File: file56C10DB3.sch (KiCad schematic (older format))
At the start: 31 parts, among them P1 BL_PAD, P10 CONN_01X01, P2 SWD_DAT, P3 SWD_CLK, P4 SWD_3V3, P5 SWD_GND, P6 SWD_RST, P7 CONN_01X01, P8 CONN_01X01, P9 CONN_01X01, U5 SAMD21E17A, Y1 32.768kHz

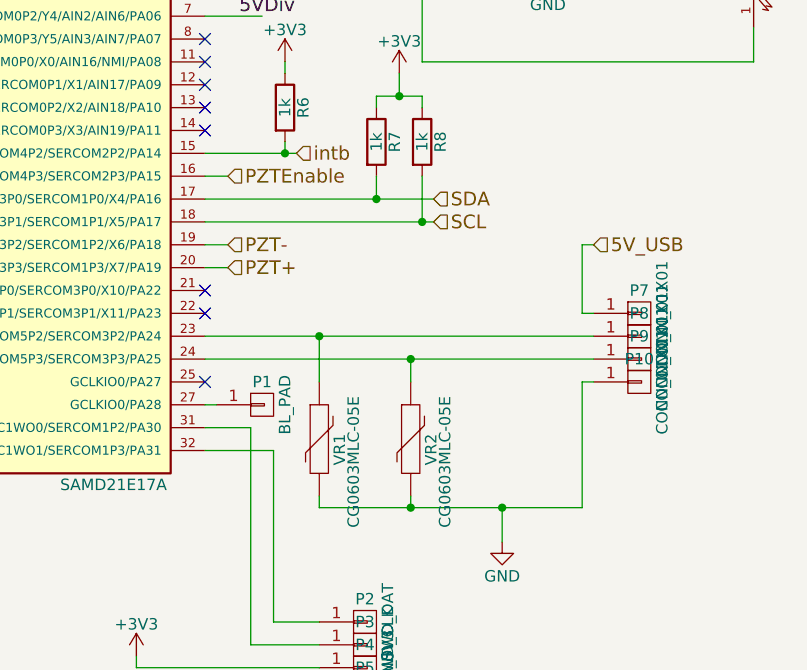
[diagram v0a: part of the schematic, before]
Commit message: Added outline for AAA battery size
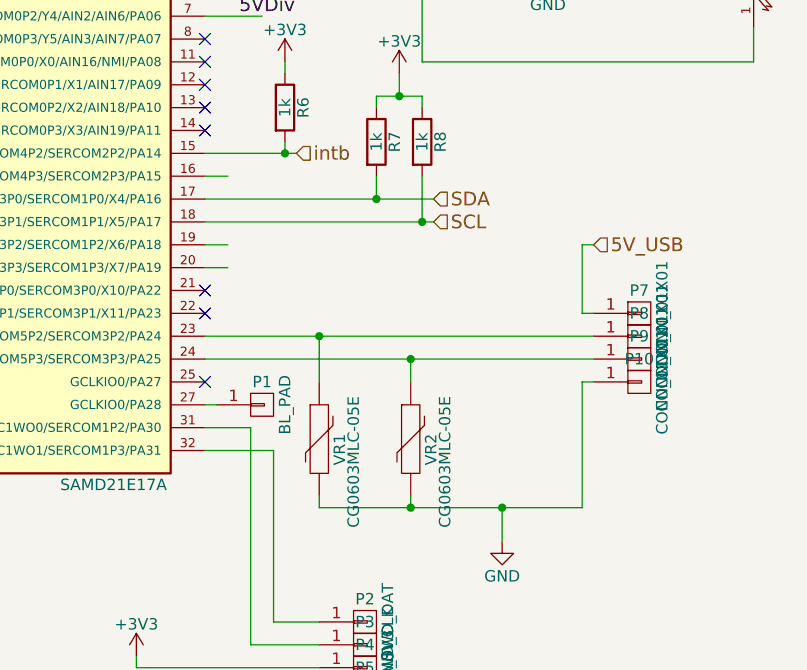
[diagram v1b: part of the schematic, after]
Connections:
- net labels removed: PZT+, PZT-, PZTEnable
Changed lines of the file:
@@
 $Descr A4 11693 8268
 encoding utf-8
-Sheet 6 6
+Sheet 6 7
 Title ""
 Date ""
@@
 Text HLabel 8050 3650 2    60   Input ~ 0
 SCL
-Text HLabel 7150 3850 2    60   Input ~ 0
-PZT+
-Text HLabel 7150 3750 2    60   Input ~ 0
-PZT-
 Text HLabel 2100 3900 0    60   Input ~ 0
 VbatIN
@@
 	8700 4050 8750 4050
 $Comp
-L GND #PWR01
+L GND #PWR15
 U 1 1 56C13132
 P 8350 5050
-F 0 "#PWR01" H 8350 4800 50  0001 C CNN
+F 0 "#PWR15" H 8350 4800 50  0001 C CNN
 F 1 "GND" H 8350 4900 50  0000 C CNN
 F 2 "" H 8350 5050 50  0000 C CNN
@@
 	8750 4350 8700 4350
 Wire Wire Line
-	8700 4350 8700 4900
+	8700 4900 8700 4350
 Wire Wire Line
 	8350 4900 8350 5050
@@
 Connection ~ 3600 2550
 $Comp
-L GND #PWR02
+L GND #PWR5
 U 1 1 56C1336E
 P 3300 3150
-F 0 "#PWR02" H 3300 2900 50  0001 C CNN
+F 0 "#PWR5" H 3300 2900 50  0001 C CNN
 F 1 "GND" H 3300 3000 50  0000 C CNN
 F 2 "" H 3300 3150 50  0000 C CNN
@@
 $EndComp
 $Comp
-L GND #PWR03
+L GND #PWR6
 U 1 1 56C133A0
 P 3600 3150
-F 0 "#PWR03" H 3600 2900 50  0001 C CNN
+F 0 "#PWR6" H 3600 2900 50  0001 C CNN
 F 1 "GND" H 3600 3000 50  0000 C CNN
 F 2 "" H 3600 3150 50  0000 C CNN
@@
 $EndComp
 $Comp
-L GND #PWR04
+L GND #PWR8
 U 1 1 56C133D2
 P 3900 3150
-F 0 "#PWR04" H 3900 2900 50  0001 C CNN
+F 0 "#PWR8" H 3900 2900 50  0001 C CNN
 F 1 "GND" H 3900 3000 50  0000 C CNN
 F 2 "" H 3900 3150 50  0000 C CNN
@@
 Wire Wire Line
 	3900 3050 3900 3150
-Text HLabel 7150 3450 2    60   Input ~ 0
-PZTEnable
 $Comp
 L R R7
@@
 $EndComp
 $Comp
-L +3V3 #PWR05
+L +3V3 #PWR14
 U 1 1 56C24D00
 P 7900 3000
-F 0 "#PWR05" H 7900 2850 50  0001 C CNN
+F 0 "#PWR14" H 7900 2850 50  0001 C CNN
 F 1 "+3V3" H 7900 3140 50  0000 C CNN
 F 2 "" H 7900 3000 50  0000 C CNN
@@
 	7950 4850 7950 4900
 Wire Wire Line
-	8700 4900 7550 4900
+	7550 4900 8700 4900
 Connection ~ 8350 4900
 Wire Wire Line
@@
 Connection ~ 8550 2250
 $Comp
-L GND #PWR06
+L GND #PWR16
 U 1 1 56C269FF
 P 8550 2550
-F 0 "#PWR06" H 8550 2300 50  0001 C CNN
+F 0 "#PWR16" H 8550 2300 50  0001 C CNN
 F 1 "GND" H 8550 2400 50  0000 C CNN
 F 2 "" H 8550 2550 50  0000 C CNN
@@
 5VDiv
 $Comp
-L GND #PWR07
+L GND #PWR1
 U 1 1 56C27864
 P 1600 4900
-F 0 "#PWR07" H 1600 4650 50  0001 C CNN
+F 0 "#PWR1" H 1600 4650 50  0001 C CNN
 F 1 "GND" H 1600 4750 50  0000 C CNN
 F 2 "" H 1600 4900 50  0000 C CNN
@@
 $EndComp
 $Comp
-L GND #PWR08
+L GND #PWR2
 U 1 1 56C278AB
 P 2350 4900
-F 0 "#PWR08" H 2350 4650 50  0001 C CNN
+F 0 "#PWR2" H 2350 4650 50  0001 C CNN
 F 1 "GND" H 2350 4750 50  0000 C CNN
 F 2 "" H 2350 4900 50  0000 C CNN
@@
 	2950 3500 2950 3700
 $Comp
-L GND #PWR09
+L GND #PWR4
 U 1 1 56C282F2
 P 2950 4100
-F 0 "#PWR09" H 2950 3850 50  0001 C CNN
+F 0 "#PWR4" H 2950 3850 50  0001 C CNN
 F 1 "GND" H 2950 3950 50  0000 C CNN
 F 2 "" H 2950 4100 50  0000 C CNN
@@
 	2950 4000 2950 4100
 $Comp
-L +3V3 #PWR010
+L +3V3 #PWR3
 U 1 1 56C28419
 P 2950 3500
-F 0 "#PWR010" H 2950 3350 50  0001 C CNN
+F 0 "#PWR3" H 2950 3350 50  0001 C CNN
 F 1 "+3V3" H 2950 3640 50  0000 C CNN
 F 2 "" H 2950 3500 50  0000 C CNN
@@
 	4000 2150 4000 2050
 $Comp
-L +3V3 #PWR011
+L +3V3 #PWR9
 U 1 1 56C28F33
 P 4000 1650
-F 0 "#PWR011" H 4000 1500 50  0001 C CNN
+F 0 "#PWR9" H 4000 1500 50  0001 C CNN
 F 1 "+3V3" H 4000 1790 50  0000 C CNN
 F 2 "" H 4000 1650 50  0000 C CNN
@@
 	7050 3350 7450 3350
 $Comp
-L +3V3 #PWR012
+L +3V3 #PWR11
 U 1 1 56C2B080
 P 6750 5550
-F 0 "#PWR012" H 6750 5400 50  0001 C CNN
+F 0 "#PWR11" H 6750 5400 50  0001 C CNN
 F 1 "+3V3" H 6750 5690 50  0000 C CNN
 F 2 "" H 6750 5550 50  0000 C CNN
@@
 $EndComp
 $Comp
-L GND #PWR013
+L GND #PWR12
 U 1 1 56C2B0D0
 P 6750 5750
-F 0 "#PWR013" H 6750 5500 50  0001 C CNN
+F 0 "#PWR12" H 6750 5500 50  0001 C CNN
 F 1 "GND" H 6750 5600 50  0000 C CNN
 F 2 "" H 6750 5750 50  0000 C CNN
@@
 	6750 5700 7550 5700
 $Comp
-L +3V3 #PWR014
+L +3V3 #PWR7
 U 1 1 56C2B3B6
 P 3750 2400
-F 0 "#PWR014" H 3750 2250 50  0001 C CNN
+F 0 "#PWR7" H 3750 2250 50  0001 C CNN
 F 1 "+3V3" H 3750 2540 50  0000 C CNN
 F 2 "" H 3750 2400 50  0000 C CNN
@@
 Connection ~ 7400 3350
 $Comp
-L +3V3 #PWR015
+L +3V3 #PWR13
 U 1 1 56C2C5C9
 P 7400 2950
-F 0 "#PWR015" H 7400 2800 50  0001 C CNN
+F 0 "#PWR13" H 7400 2800 50  0001 C CNN
 F 1 "+3V3" H 7400 3090 50  0000 C CNN
 F 2 "" H 7400 2950 50  0000 C CNN
@@
 NoConn ~ 7050 2350
 $Comp
-L GND #PWR016
+L GND #PWR10
 U 1 1 56C39EB2
 P 4300 4800
-F 0 "#PWR016" H 4300 4550 50  0001 C CNN
+F 0 "#PWR10" H 4300 4550 50  0001 C CNN
 F 1 "GND" H 4300 4650 50  0000 C CNN
 F 2 "" H 4300 4800 50  0000 C CNN
@@
 	9450 2950 9450 2800
 $Comp
-L +3V3 #PWR017
+L +3V3 #PWR17
 U 1 1 56C3A13C
 P 9450 1850
-F 0 "#PWR017" H 9450 1700 50  0001 C CNN
+F 0 "#PWR17" H 9450 1700 50  0001 C CNN
 F 1 "+3V3" H 9450 1990 50  0000 C CNN
 F 2 "" H 9450 1850 50  0000 C CNN

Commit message: started layout, completed schematic
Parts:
- removed R1: 10k, Capacitors_SMD:C_0603, symbol R
- removed R2: 2k, Capacitors_SMD:C_0603, symbol R
- removed R6: 1k, Capacitors_SMD:C_0603, symbol R
- added P11: CONN_01X04, symbol CONN_01X04
- L1: value MH2029-300Y -> 100R; footprint Capacitors_SMD:C_0805 -> ~
- renumbered C3 to C10, C4 to C11, C5 to C12, C6 to C13, C1 to C8, C2 to C9, R5 to R1, R3 to R2, R4 to R3, R9 to R4, R7 to R5, R8 to R6, U5 to U4
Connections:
- net labels added: +3.3V, AIN_6, MPU_D14, MPU_IN14, MPU_INT4, MPU_INT5, MPU_INT9, MPU_MISO, MPU_MOSI, MPU_RX1, MPU_SCK, MPU_SCL, MPU_SDA, MPU_SS, MPU_TX1
- net labels removed: 5VDiv, 5VSenseIn, 5V_USB, SCL, SDA, VbatDiv, intb
- wire segments 85 -> 96
- no-connect marks 10 -> 4
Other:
- moved on the sheet: C10, C11, C12, C13, C8, C9, D1, L1, P1, P10, P2, P3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
